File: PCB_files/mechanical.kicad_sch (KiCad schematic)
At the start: 27 parts, among them J5 CM4-A, J6 CM4-B, J7 HDMI_ribbon

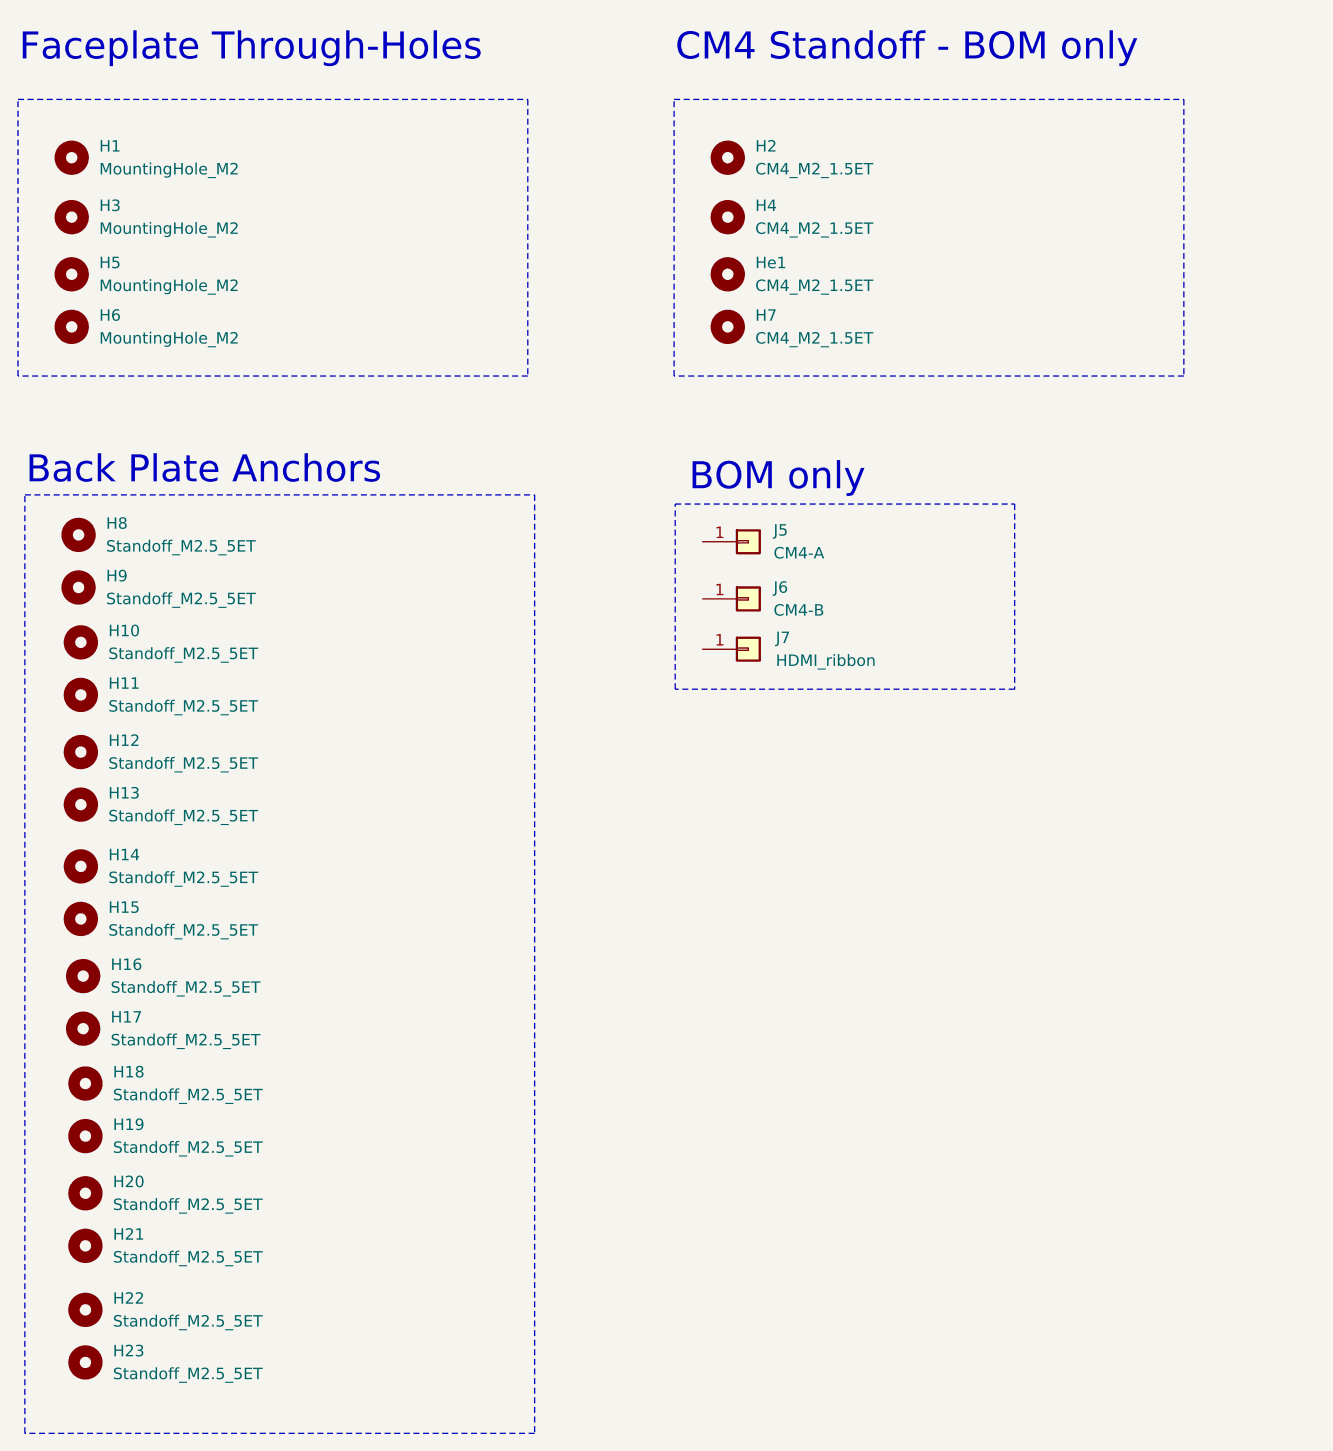
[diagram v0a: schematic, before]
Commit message: final BOM and tweaking
Tweaked some dimensions after mechanical assembly. Generated BOM and reviewed against reseller inventory
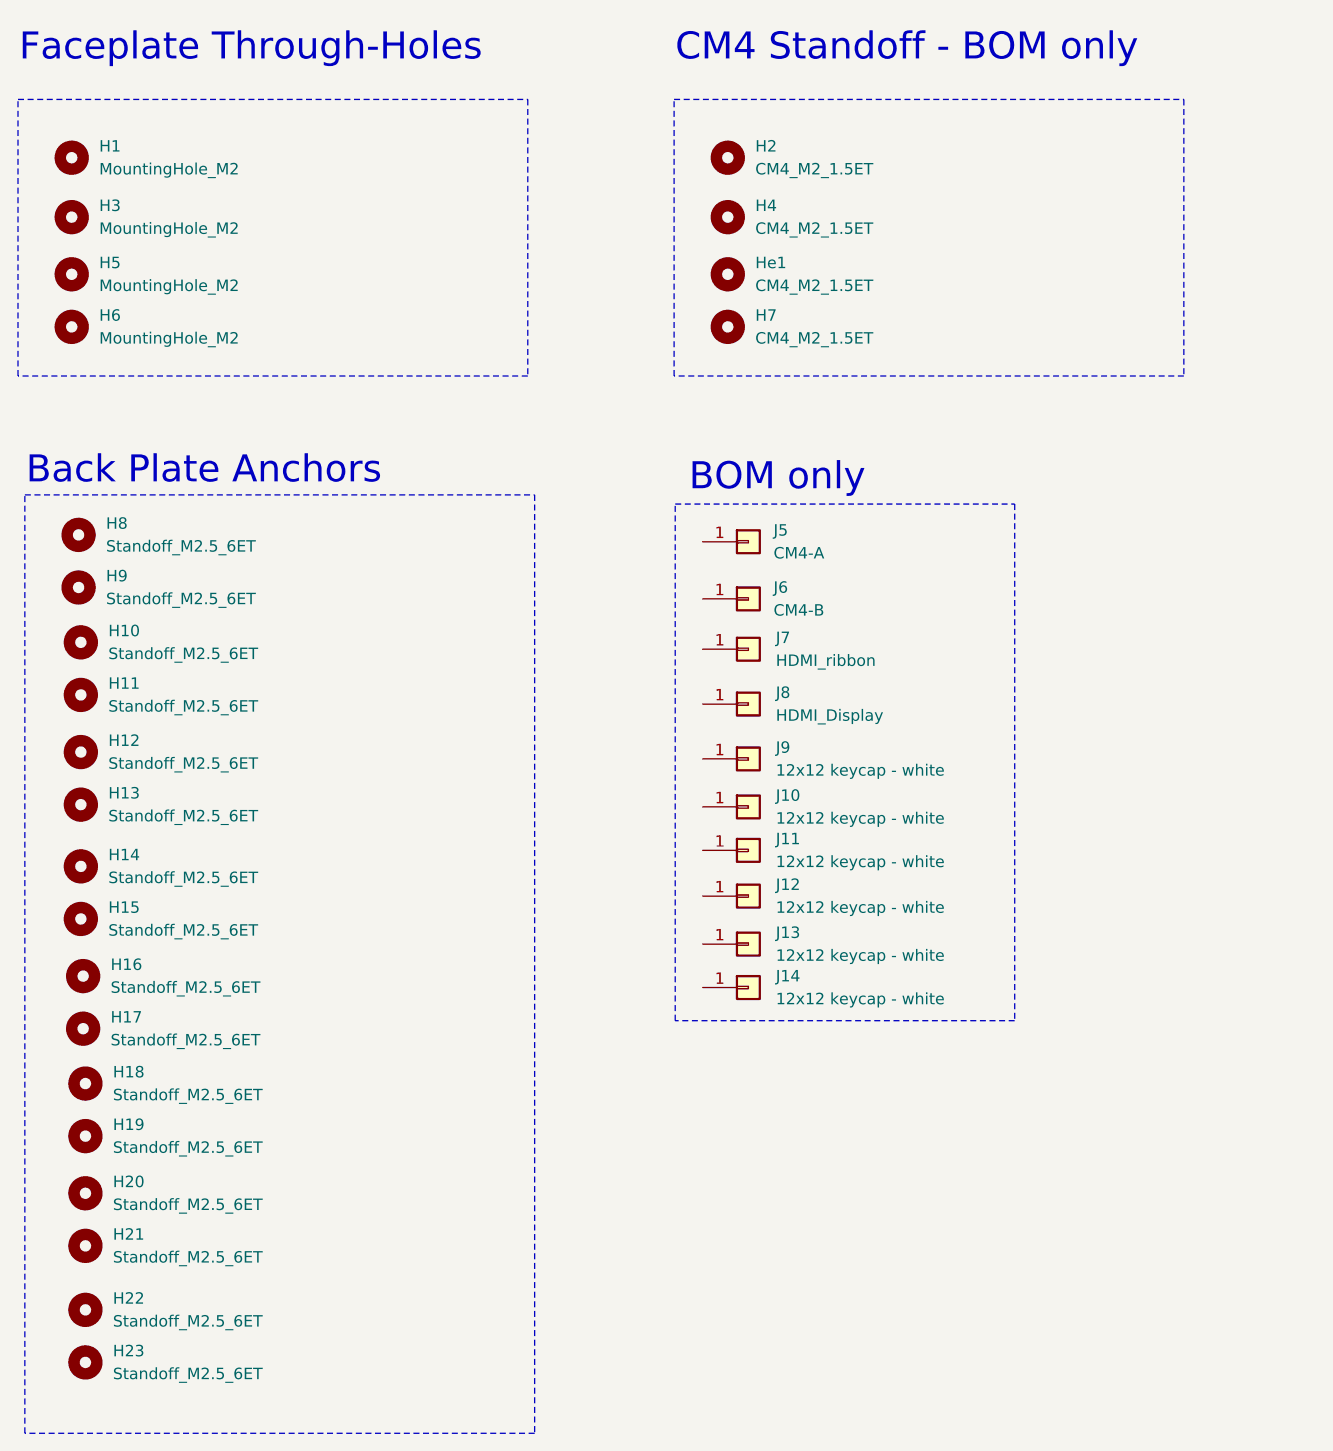
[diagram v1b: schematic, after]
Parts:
- added J10, J11, J12, J13, J14, J9: 12x12 keycap - white, N/A, symbol Connector_Generic:Conn_01x01
- added J8: HDMI_Display, N/A, symbol Connector_Generic:Conn_01x01
- H1, H3, H5, H6: Mouser_PN N/A -> (none); Reseller_P/N (none) -> N/A; Source/Reseller (none) -> N/A
- H10, H11, H12, H13, H14, H15, H16, H17, H18, H19, H20, H21, H22, H23, H8, H9: value Standoff_M2.5_5ET -> Standoff_M2.5_6ET; footprint user:Standoff_M2.5_5ET -> user:Standoff_M2.5_6ET; MPN (none) -> SMTSO-M25-6ET; Manufacturer (none) -> PEM; Mouser_PN 153-SMTSO-M25-3ET -> (none); Reseller_P/N (none) -> 153-SMTSO-M25-6ET; Source/Reseller (none) -> Mouser
- H2, H4, H7, He1: MPN (none) -> 9774015243R; Manufacturer (none) -> Wurth; Mouser_PN 710-9774015243R -> (none); Reseller_P/N (none) -> 710-9774015243R; Source/Reseller (none) -> Mouser
- J5, J6: MPN (none) -> DF40C-100DS-0.4V(51); Manufacturer (none) -> Hirose; Mouser_PN 798-DF40C100DS0.4V51 -> (none); Reseller_P/N (none) -> 798-DF40C100DS0.4V51; Source/Reseller (none) -> Mouser
- J7: MPN (none) -> 05-40-D-0152-A-4-06-4-G; Manufacturer (none) -> GCT; Mouser_PN 640-540-D0152A4064T -> (none); Reseller_P/N (none) -> 640-540-D0152A4064T; Source/Reseller (none) -> Mouser
